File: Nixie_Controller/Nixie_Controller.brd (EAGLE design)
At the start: 150 x 100 mm, 61 parts, among them IC1 4028N, T1 MMBTA42, T10 MMBTA42, T11 MMBTA42, T12 MMBTA42, T13 MMBTA42, T14 MMBTA42, T2 MMBTA42, T3 MMBTA42, T4 MMBTA42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

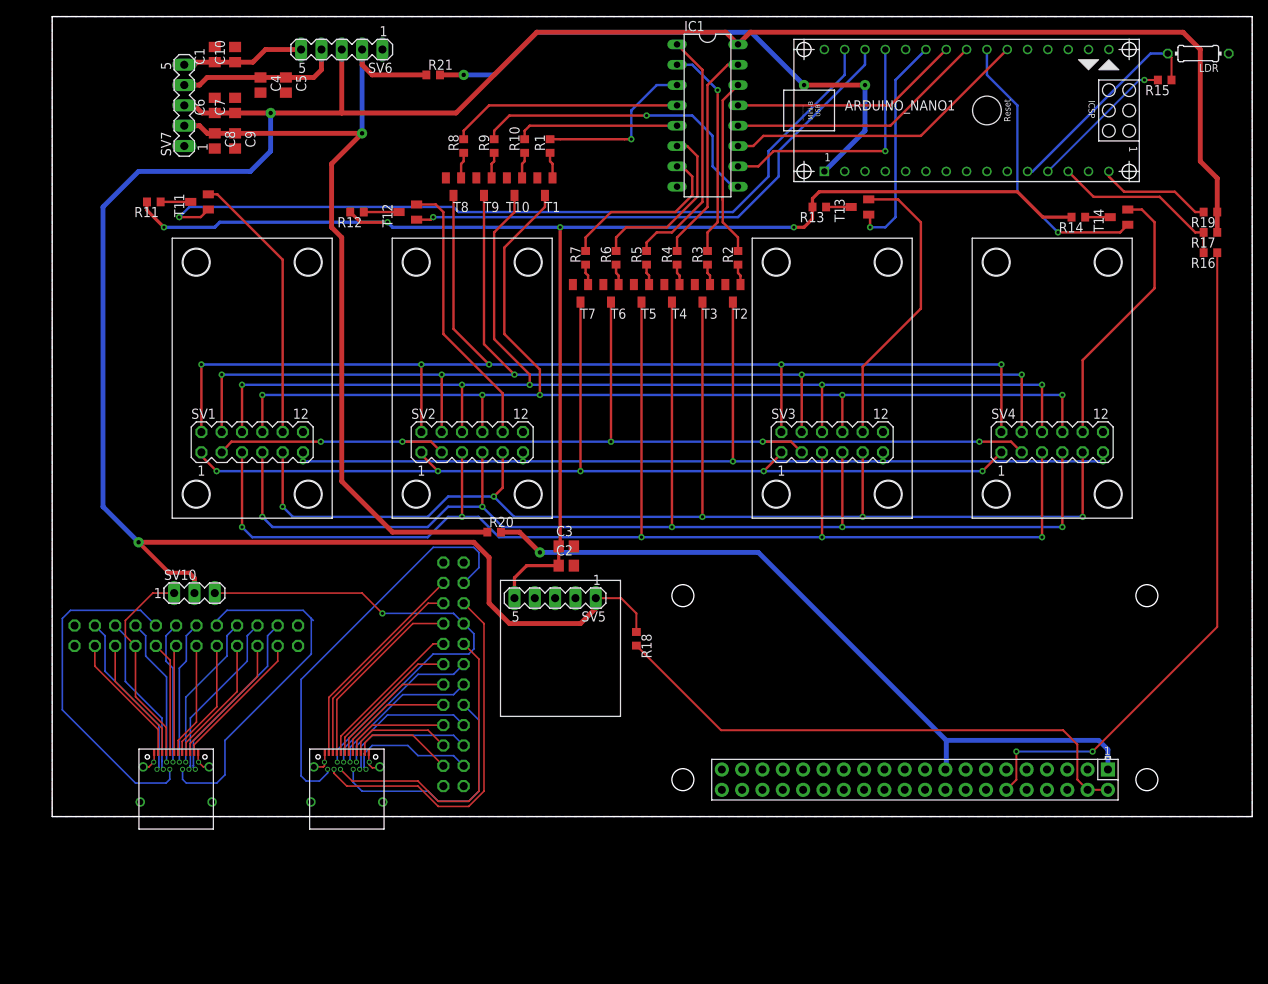
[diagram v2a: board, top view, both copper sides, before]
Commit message: fix: reroute multiple wires
Rerouted multiple wires and moved a few components, mainly for aesthetic reasons
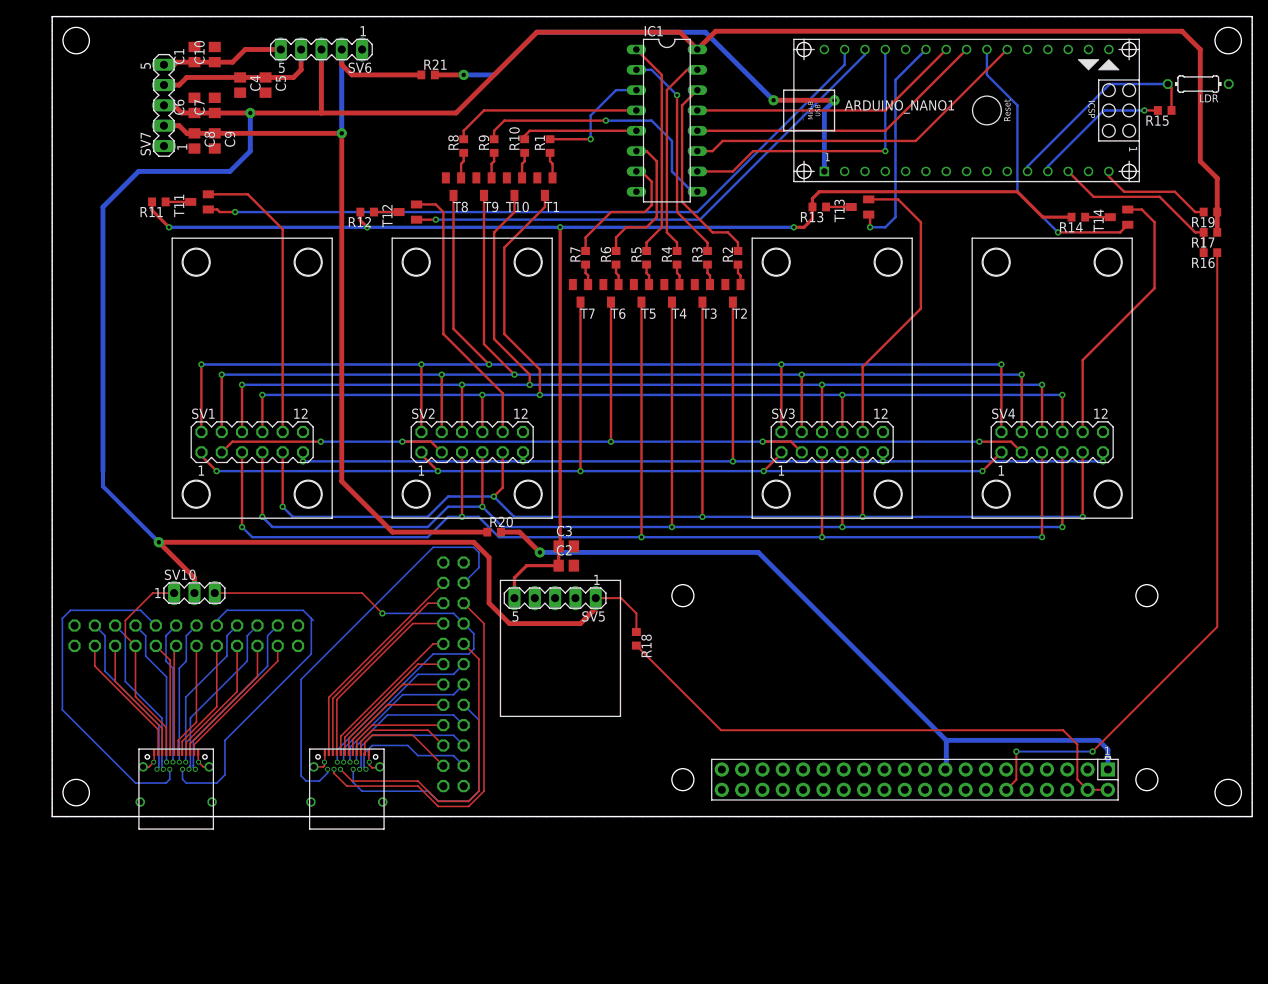
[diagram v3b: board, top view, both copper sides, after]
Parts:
- moved IC1 5.12 mm to (76.8, 87.0)
- moved LDR 3.81 mm to (143.3, 91.6)
- moved R15 3.81 mm to (139.1, 88.3)
- moved SV7 2.54 mm to (14.0, 88.9)
- moved C1 2.54 mm to (17.8, 95.2)
- moved C10 2.54 mm to (20.3, 95.2)
- moved C4 2.54 mm to (23.5, 91.4)
- moved C5 2.54 mm to (26.7, 91.4)
- moved C6 2.54 mm to (17.8, 88.9)
- moved C7 2.54 mm to (20.3, 88.9)
- moved C8 2.54 mm to (17.8, 84.5)
- moved C9 2.54 mm to (20.3, 84.5)
- moved SV6 2.54 mm to (33.7, 95.9)
- moved R12 1.27 mm to (39.4, 75.6)
- moved R11 0.64 mm to (13.3, 76.8)
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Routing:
- net N$46: track 100.1 -> 89.2 mm
- net N$39: track 71.0 -> 65.1 mm
- net N$10: track 20.4 -> 14.7 mm
- net N$1: track 20.8 -> 15.1 mm
- net N$125: track 31.9 -> 37.2 mm
- net N$123: track 32.5 -> 37.9 mm
- net N$122: track 38.7 -> 44.0 mm
- net N$8: track 29.0 -> 23.7 mm
- net N$124: track 28.9 -> 34.3 mm
- net N$9: track 38.2 -> 32.9 mm
- net N$7: track 22.0 -> 17.0 mm
- net N$6: track 22.1 -> 17.9 mm
- net +170V: track 179.6 -> 175.5 mm
- net N$5: track 31.1 -> 27.3 mm
- net VDD: track 323.5 -> 320.1 mm
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
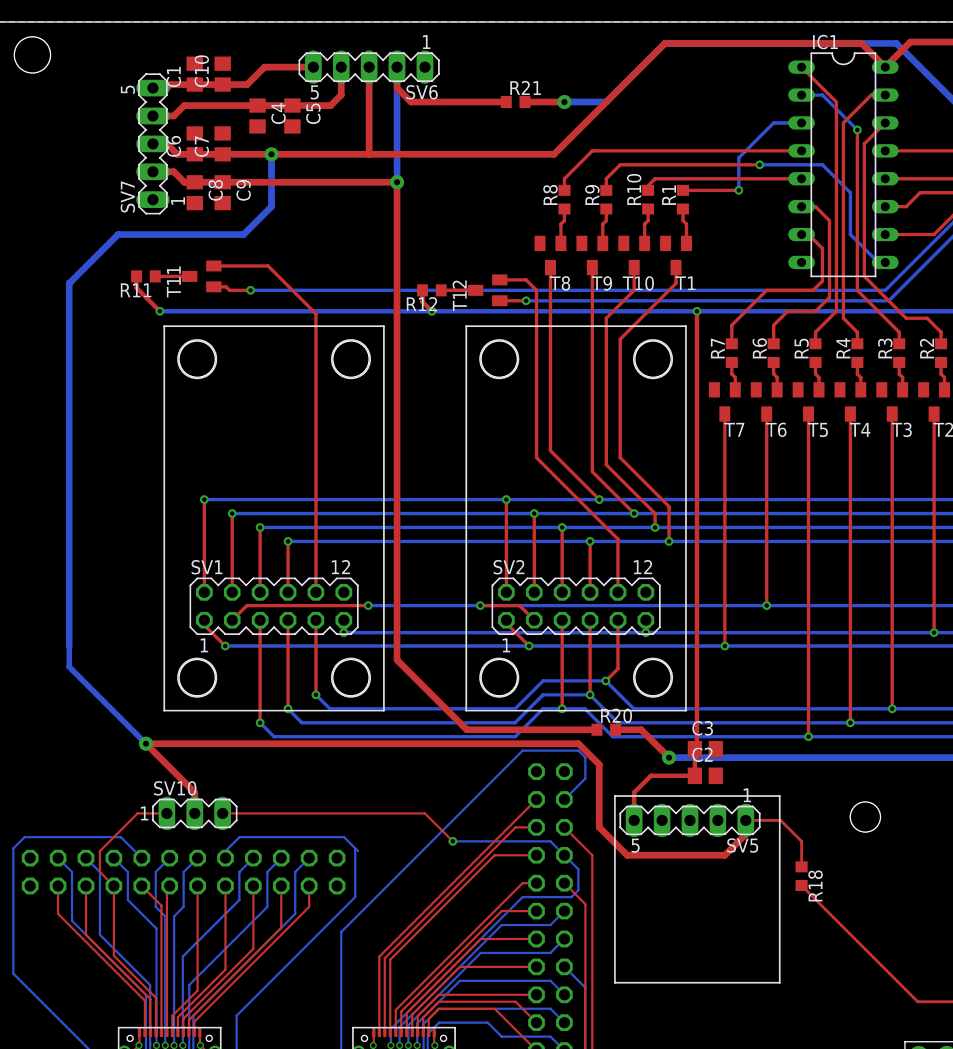
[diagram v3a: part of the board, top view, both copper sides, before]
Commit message: fix: add supply vias
Add a few vias to the supply connections, to be able to solder additional wires to the supply connections if needed
Reroute a few traces
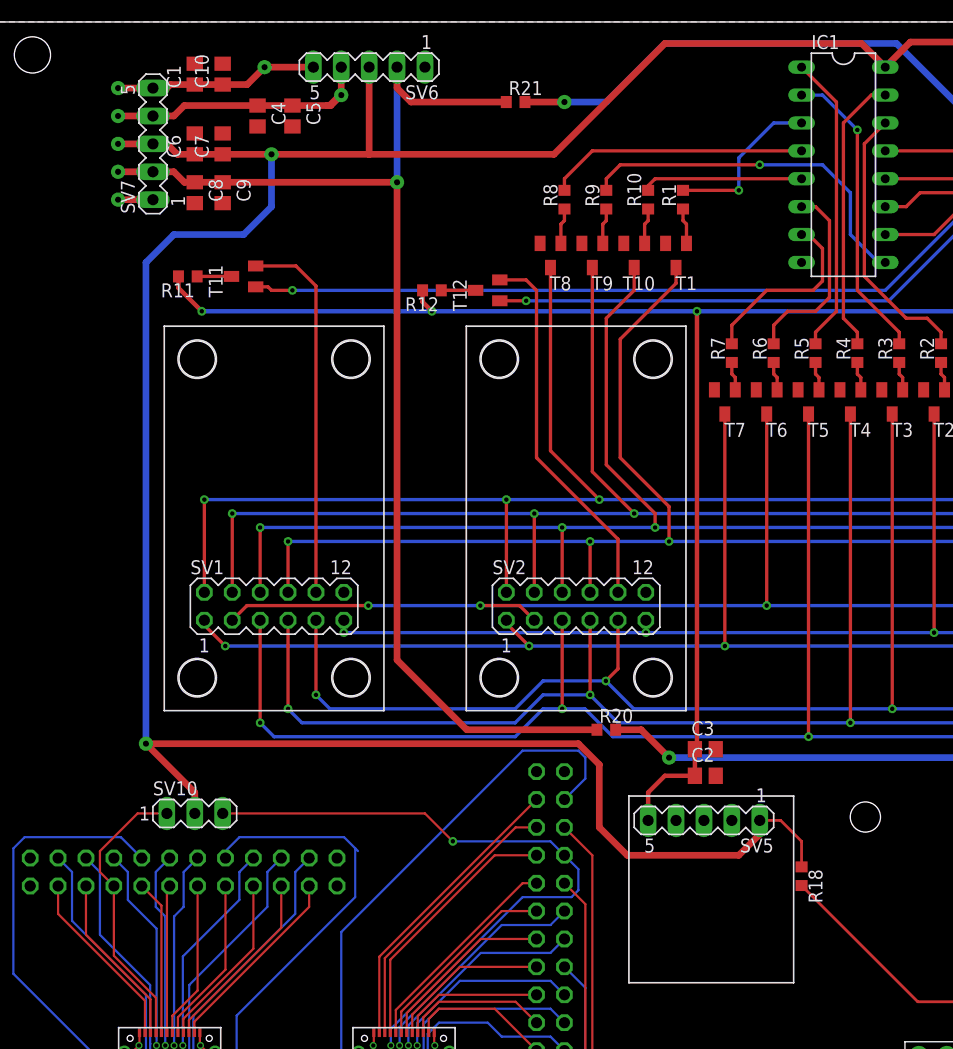
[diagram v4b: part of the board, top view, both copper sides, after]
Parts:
- moved T11 3.81 mm to (22.2, 76.8)
- moved R11 3.81 mm to (17.1, 76.8)
- moved SV5 1.27 mm to (64.1, 27.3)
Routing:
- net VDD: track 320.1 -> 314.5 mm, vias 2 -> 3
- net +170V: track 175.5 -> 170.4 mm
- net +12V: track 20.5 -> 25.3 mm, vias 0 -> 2
- net N$46: track 89.2 -> 85.4 mm
- net GND: track 11.8 -> 15.0 mm, vias 0 -> 1
- net +24V: track 15.4 -> 18.6 mm, vias 0 -> 2
- net +3V3: track 109.8 -> 113.0 mm, vias 1 -> 2
- net N$38: track 36.5 -> 34.1 mm

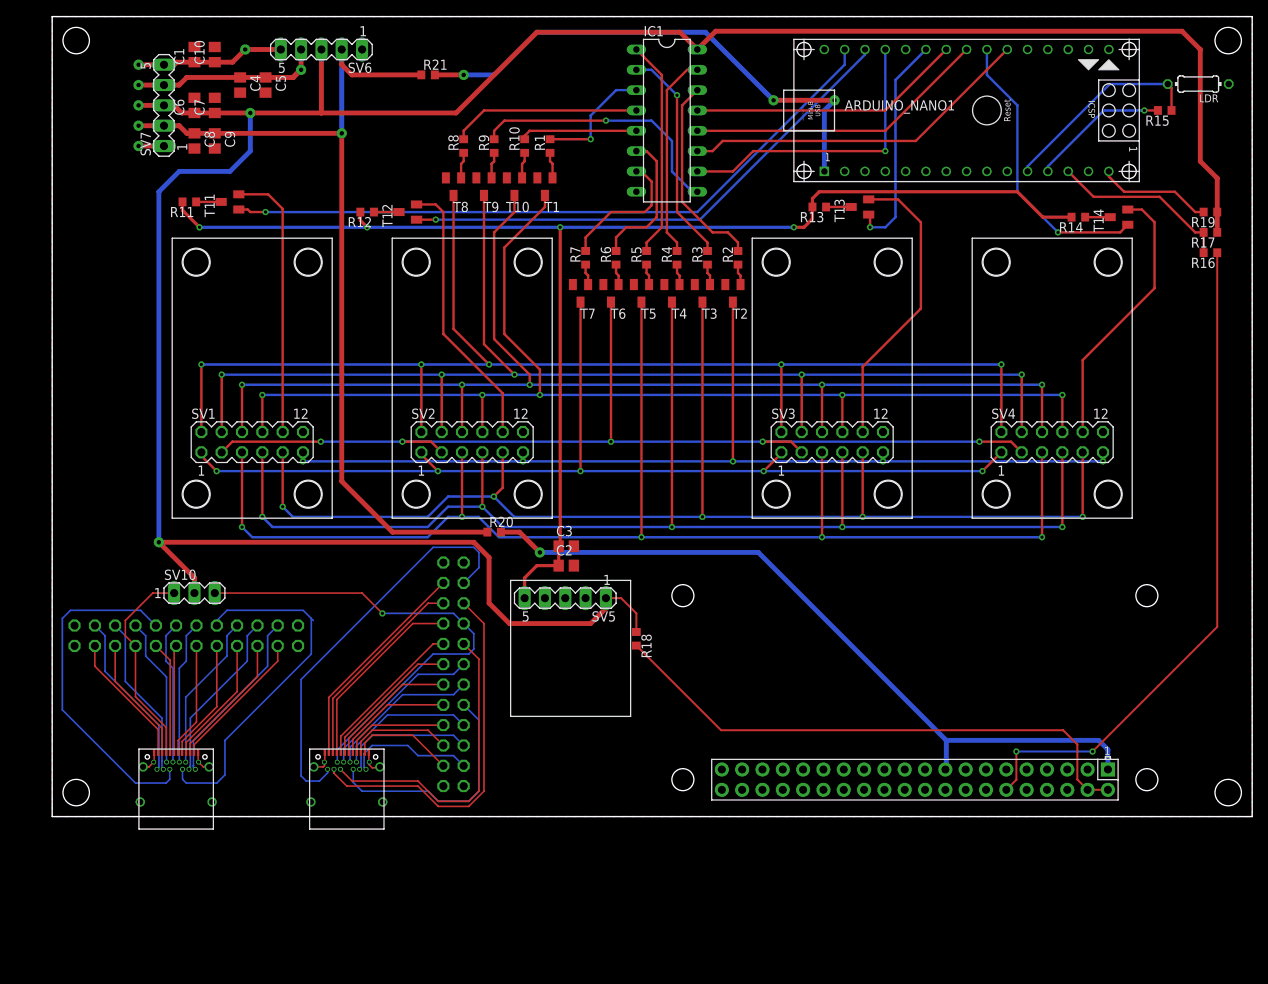
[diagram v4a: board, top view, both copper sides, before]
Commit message: feat: Add double anode nixie support
Add support for nixie tubes that use two anodes.
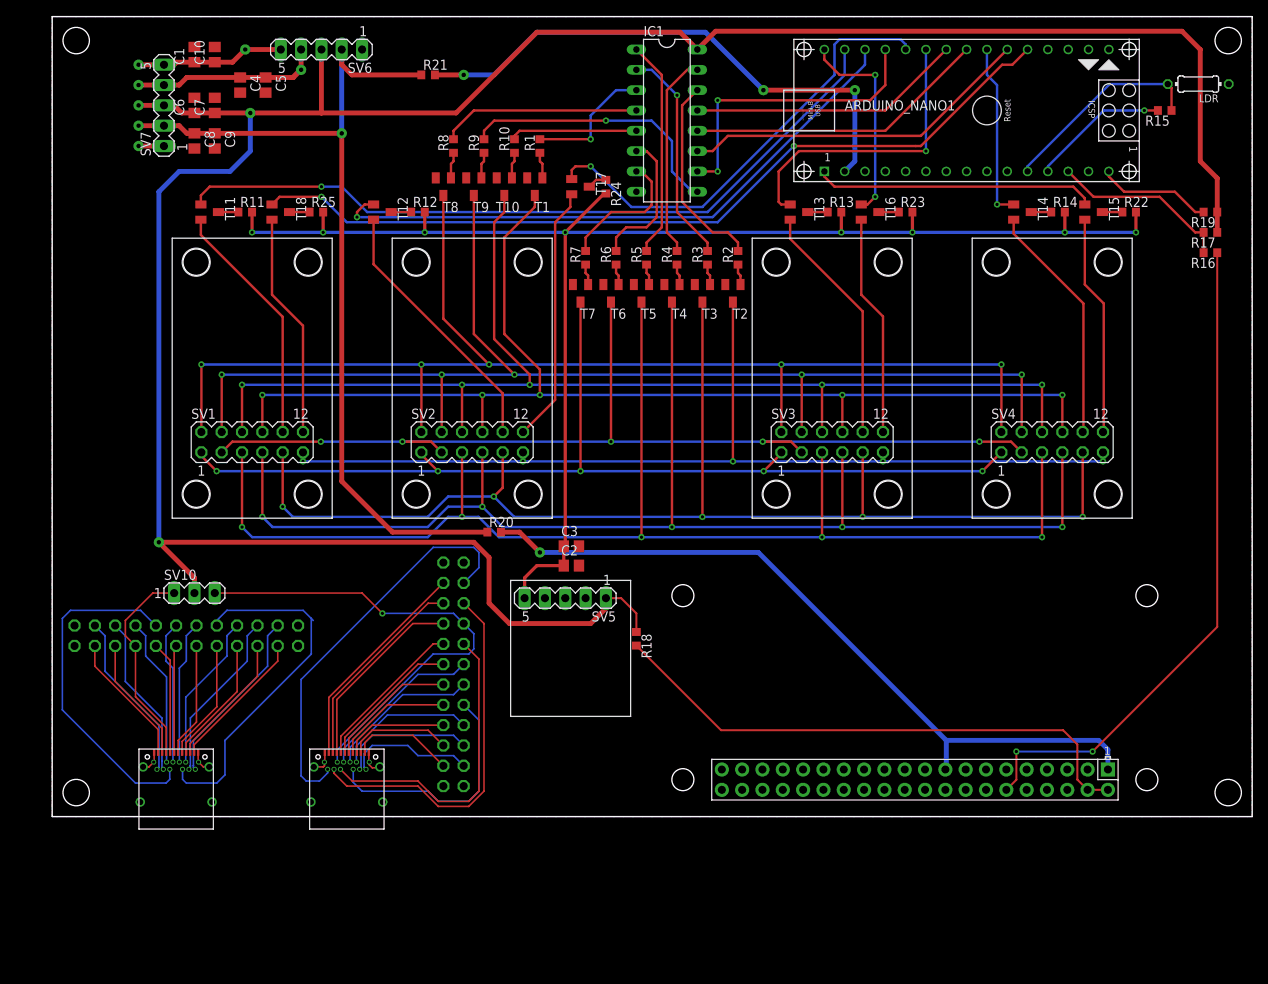
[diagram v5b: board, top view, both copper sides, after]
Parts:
- added R22, R23, R24, R25: 22k, resistor:R0603
- added T15, T16, T17, T18: MMBTA42, transistor:SOT23
- moved T14 12.1 mm to (121.3, 75.6), turned to 270 degrees
- moved T13 7.65 mm to (93.3, 75.6), turned to 270 degrees
- moved R11 7.10 mm to (24.1, 75.6), turned to 0 degrees
- moved R12 6.35 mm to (45.7, 75.6), turned to 0 degrees
- moved T12 3.18 mm to (41.3, 75.6), turned to 270 degrees
- moved T11 2.84 mm to (19.7, 75.6), turned to 270 degrees
- moved R14 2.62 mm to (125.7, 75.6), turned to 0 degrees
- moved R13 2.01 mm to (97.8, 75.6), turned to 0 degrees
- moved R10 1.27 mm to (57.8, 83.8)
- moved R8 1.27 mm to (50.2, 83.8)
- moved T9 1.27 mm to (52.7, 78.7)
- moved R1 1.27 mm to (61.0, 83.8)
- moved R9 1.27 mm to (54.0, 83.8)
- moved T1 1.27 mm to (60.3, 78.7)
- moved T10 1.27 mm to (56.5, 78.7)
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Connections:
- new net N$101: ARDUINO_NANO1.1, T15.1
- new net N$102: ARDUINO_NANO1.20, T18.1
- new net N$103: ARDUINO_NANO1.26, T17.1
- new net N$104: ARDUINO_NANO1.30, T16.1
- new net N$57: R22.1, T15.3
- new net N$58: R25.1, T18.3
- new net N$69: R24.1, T17.3
- new net N$70: R23.1, T16.3
- new net N$76: SV4.12, T15.2
- new net N$82: SV3.12, T16.2
- new net N$88: SV2.12, T17.2
- new net N$95: SV1.12, T18.2
- net +170V: now also R22.2, R23.2, R24.2, R25.2
- net N$39: now also ARDUINO_NANO1.2; no longer ARDUINO_NANO1.1
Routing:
- net N$102: track 0.00 -> 105.1 mm, vias 0 -> 2
- net N$103: track 0.00 -> 57.0 mm, vias 0 -> 1
- net N$101: track 0.00 -> 35.1 mm
- net N$88: track 0.00 -> 32.2 mm
- net N$95: track 0.00 -> 28.2 mm
- net N$82: track 0.00 -> 27.7 mm
- net N$76: track 0.00 -> 27.6 mm
- net N$104: track 0.00 -> 25.8 mm, vias 0 -> 2
- net +170V: track 170.4 -> 185.2 mm, vias 4 -> 8
- net N$49: track 35.7 -> 22.0 mm
- net N$40: track 65.2 -> 76.4 mm
- net N$48: track 27.9 -> 37.5 mm
- net N$46: track 85.4 -> 93.6 mm
- net N$36: track 36.9 -> 30.3 mm
- net N$35: track 33.9 -> 30.2 mm
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
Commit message: fix: Remove DRC errors
Remove the erros the DRC mentioned.
Reroute and move multiple components for a cleaner look.
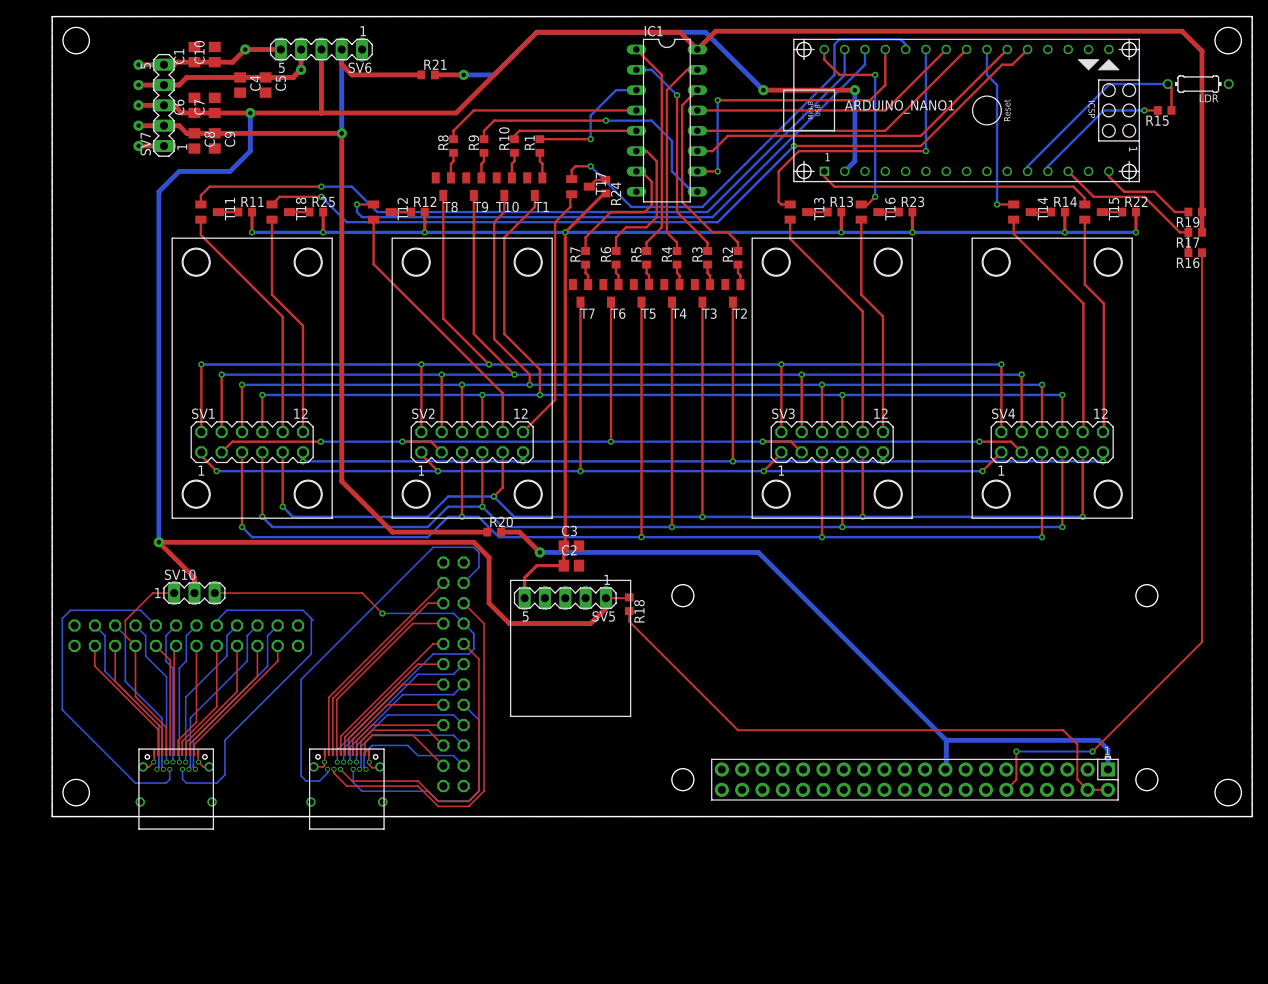
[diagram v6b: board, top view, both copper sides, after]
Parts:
- moved R18 4.41 mm to (72.1, 26.5)
- moved R16 1.91 mm to (142.9, 70.5)
- moved R17 1.91 mm to (142.9, 73.0)
- moved R19 1.91 mm to (142.9, 75.6)
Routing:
- net VDD: track 314.5 -> 309.7 mm
- net +5V: track 69.0 -> 72.4 mm
- net N$96: track 14.3 -> 12.4 mm
- net N$43: track 22.6 -> 20.7 mm
- net N$94: track 83.6 -> 82.9 mm
